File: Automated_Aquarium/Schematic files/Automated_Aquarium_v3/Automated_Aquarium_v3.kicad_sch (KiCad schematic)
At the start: 0 parts

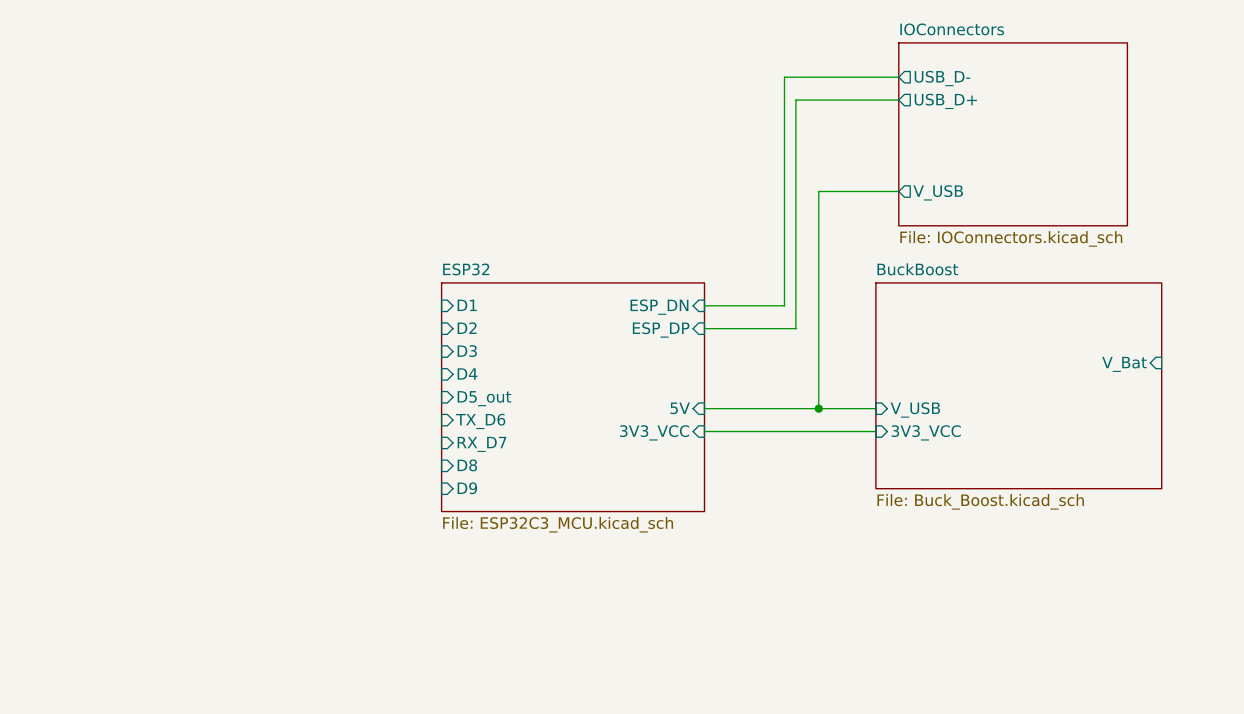
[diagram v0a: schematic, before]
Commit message: complete 0v1 layout aquarium
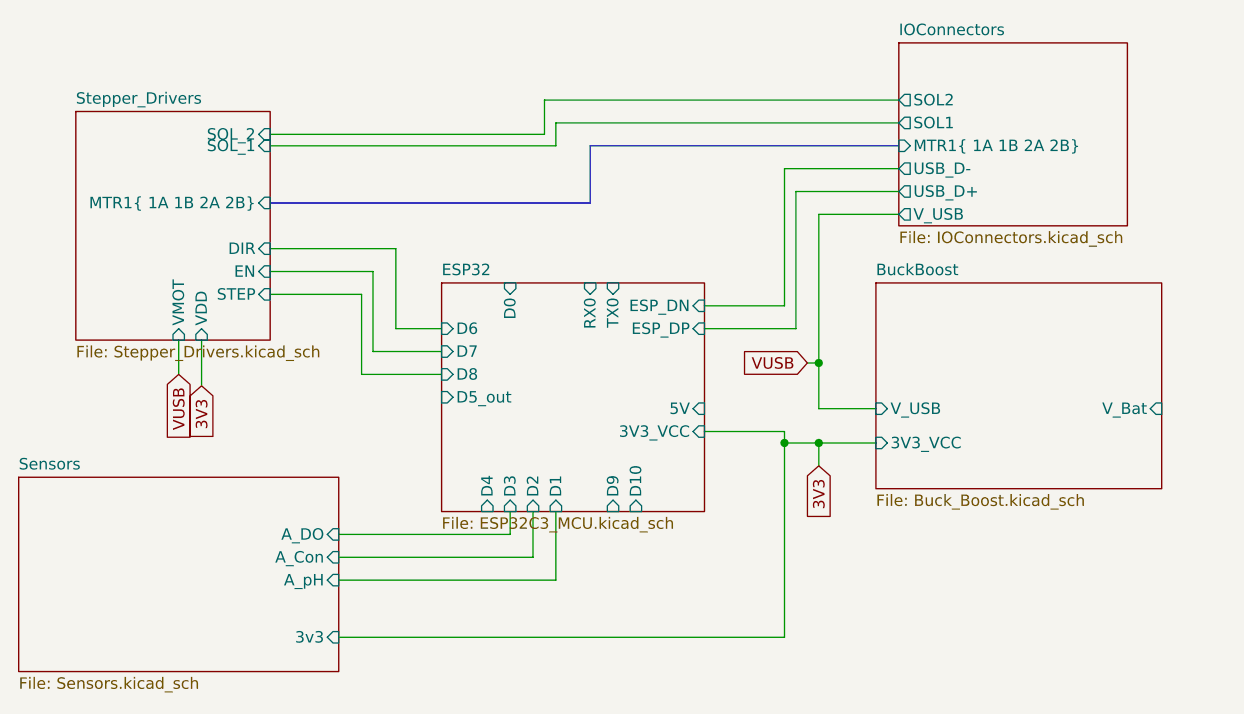
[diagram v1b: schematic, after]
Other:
- added sheet Sensors (Sensors.kicad_sch)
- added sheet Stepper_Drivers (Stepper_Drivers.kicad_sch)
- sheet ESP32 ports: added D0, D10, D6, D7, RX0, TX0; removed RX_D7, TX_D6
- sheet IOConnectors ports: added MTR1{ 1A 1B 2A 2B}, SOL1, SOL2; removed none

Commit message: finish aqua schem, add inital layout
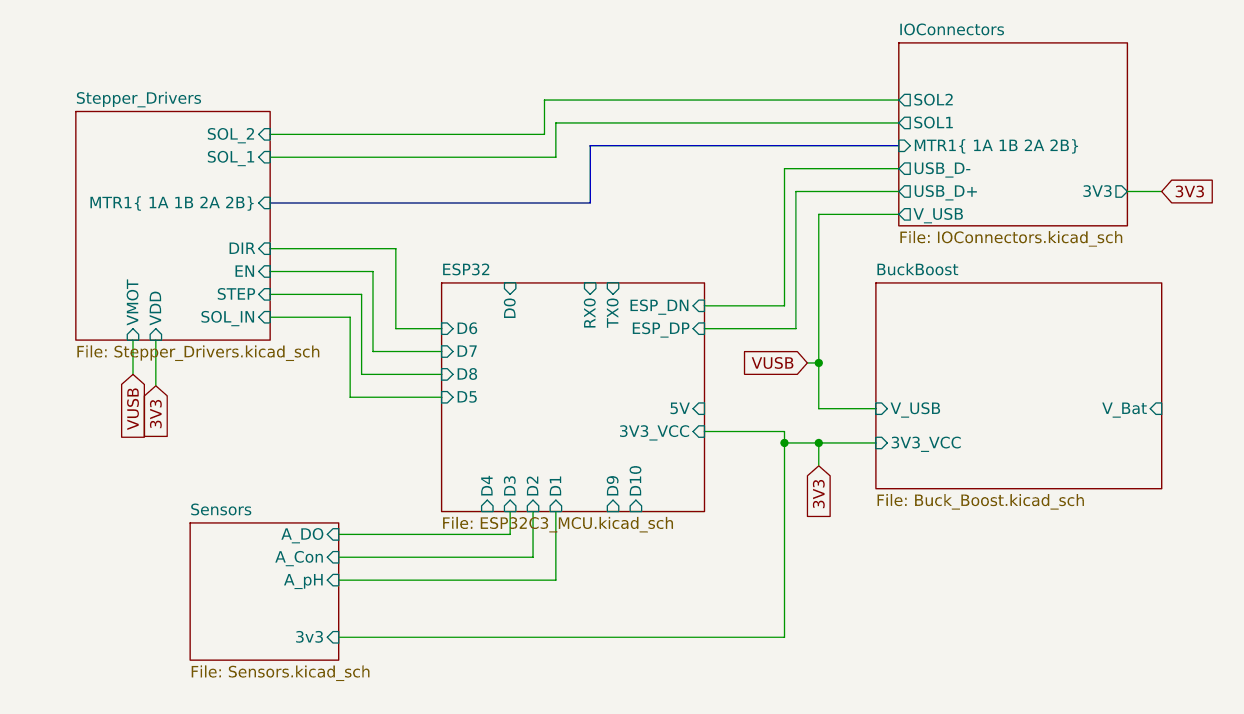
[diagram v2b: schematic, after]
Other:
- sheet ESP32 ports: added D5; removed D5_out
- sheet IOConnectors ports: added 3V3; removed none
- sheet Stepper_Drivers ports: added SOL_IN; removed none
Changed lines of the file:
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@@
+    (stroke (width 0) (type default))
+  )
+  (wire (pts (xy 81.28 63.5) (xy 90.17 63.5))
     (stroke (width 0) (type default))
   )
@@
     (stroke (width 0) (type default))
   )
+  (wire (pts (xy 90.17 72.39) (xy 100.33 72.39))
+    (stroke (width 0) (type default))
+  )
   (bus (pts (xy 116.84 50.8) (xy 81.28 50.8))
     (stroke (width 0) (type default))
   )
-  (wire (pts (xy 81.28 44.45) (xy 113.03 44.45))
+  (wire (pts (xy 81.28 45.72) (xy 113.03 45.72))
     (stroke (width 0) (type default))
   )
@@
     (stroke (width 0) (type default))
   )
+  (wire (pts (xy 176.53 49.53) (xy 180.34 49.53))
+    (stroke (width 0) (type default))
+  )
   (wire (pts (xy 138.43 99.06) (xy 138.43 77.47))
     (stroke (width 0) (type default))
@@
     (stroke (width 0) (type default))
   )
-  (wire (pts (xy 71.12 66.04) (xy 71.12 69.85))
+  (wire (pts (xy 66.04 66.04) (xy 66.04 69.85))
     (stroke (width 0) (type default))
   )
@@
     (stroke (width 0) (type default))
   )
+  (wire (pts (xy 90.17 63.5) (xy 90.17 72.39))
+    (stroke (width 0) (type default))
+  )
   (wire (pts (xy 88.9 87.63) (xy 107.95 87.63))
     (stroke (width 0) (type default))
@@
     (stroke (width 0) (type default))
   )
-  (wire (pts (xy 113.03 44.45) (xy 113.03 41.91))
+  (wire (pts (xy 113.03 45.72) (xy 113.03 41.91))
     (stroke (width 0) (type default))
   )
@@
     (stroke (width 0) (type default))
   )
-  (wire (pts (xy 73.66 66.04) (xy 73.66 71.12))
+  (wire (pts (xy 68.58 66.04) (xy 68.58 71.12))
     (stroke (width 0) (type default))
   )
@@
     )
   )
-  (global_label "3V3" (shape input) (at 73.66 71.12 270) (fields_autoplaced)
+  (global_label "3V3" (shape input) (at 180.34 49.53 0) (fields_autoplaced)
+    (effects (font (size 1.27 1.27)) (justify left))
+    (property "Intersheetrefs" "${INTERSHEET_REFS}" (at 186.7534 49.53 0)
+      (effects (font (size 1.27 1.27)) (justify left) hide)
+    )
+  )
+  (global_label "3V3" (shape input) (at 68.58 71.12 270) (fields_autoplaced)
     (effects (font (size 1.27 1.27)) (justify right))
-    (property "Intersheetrefs" "${INTERSHEET_REFS}" (at 73.66 77.5334 90)
+    (property "Intersheetrefs" "${INTERSHEET_REFS}" (at 68.58 77.5334 90)
       (effects (font (size 1.27 1.27)) (justify right) hide)
     )
   )
-  (global_label "VUSB" (shape input) (at 71.12 69.85 270) (fields_autoplaced)
+  (global_label "VUSB" (shape input) (at 66.04 69.85 270) (fields_autoplaced)
     (effects (font (size 1.27 1.27)) (justify right))
-    (property "Intersheetrefs" "${INTERSHEET_REFS}" (at 71.12 77.6544 90)
+    (property "Intersheetrefs" "${INTERSHEET_REFS}" (at 66.04 77.6544 90)
       (effects (font (size 1.27 1.27)) (justify right) hide)
     )
@@
       (effects (font (size 1.27 1.27)) (justify right))
     )
-    (pin "VDD" input (at 73.66 66.04 270)
-      (effects (font (size 1.27 1.27)) (justify left))
-    )
-    (pin "VMOT" input (at 71.12 66.04 270)
+    (pin "VDD" input (at 68.58 66.04 270)
+      (effects (font (size 1.27 1.27)) (justify left))
+    )
+    (pin "VMOT" input (at 66.04 66.04 270)
       (effects (font (size 1.27 1.27)) (justify left))
     )
@@
       (effects (font (size 1.27 1.27)) (justify right))
     )
-    (pin "SOL_1" input (at 81.28 44.45 0)
+    (pin "SOL_1" input (at 81.28 45.72 0)
       (effects (font (size 1.27 1.27)) (justify right))
     )
     (pin "SOL_2" input (at 81.28 43.18 0)
+      (effects (font (size 1.27 1.27)) (justify right))
+    )
+    (pin "SOL_IN" input (at 81.28 63.5 0)
       (effects (font (size 1.27 1.27)) (justify right))
     )
@@
       (effects (font (size 1.27 1.27)) (justify left))
     )
-    (pin "D5_out" input (at 100.33 72.39 180)
-      (effects (font (size 1.27 1.27)) (justify left))
-    )
     (pin "D4" input (at 105.41 85.09 270)
       (effects (font (size 1.27 1.27)) (justify left))
@@
     (pin "TX0" input (at 119.38 59.69 90)
       (effects (font (size 1.27 1.27)) (justify right))
+    )
+    (pin "D5" input (at 100.33 72.39 180)
+      (effects (font (size 1.27 1.27)) (justify left))
     )
     (instances
@@
     )
   )
-  (sheet (at 53.34 81.28) (size 35.56 21.59) (fields_autoplaced)
-    (stroke (width 0.1524) (type solid))
-    (fill (color 0 0 0 0.0000))
-    (property "Sheetname" "Sensors" (at 53.34 80.5684 0)
-      (effects (font (size 1.27 1.27)) (justify left bottom))
-    )
-    (property "Sheetfile" "Sensors.kicad_sch" (at 53.34 103.4546 0)
+  (sheet (at 72.39 86.36) (size 16.51 15.24) (fields_autoplaced)
+    (stroke (width 0.1524) (type solid))
+    (fill (color 0 0 0 0.0000))
+    (property "Sheetname" "Sensors" (at 72.39 85.6484 0)
+      (effects (font (size 1.27 1.27)) (justify left bottom))
+    )
+    (property "Sheetfile" "Sensors.kicad_sch" (at 72.39 102.1846 0)
       (effects (font (size 1.27 1.27)) (justify left top))
     )
@@
       (effects (font (size 1.27 1.27)) (justify left))
     )
-    (instances
+    (pin "3V3" output (at 176.53 49.53 0)
+      (effects (font (size 1.27 1.27)) (justify right))
+    )
+    (instances
